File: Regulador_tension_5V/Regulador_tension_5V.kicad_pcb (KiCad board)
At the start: 2 copper layers, 53.6 x 29.2 mm, 10 parts, among them P1 CONN_01X02, P2 CONN_01X02, U1 LM7805

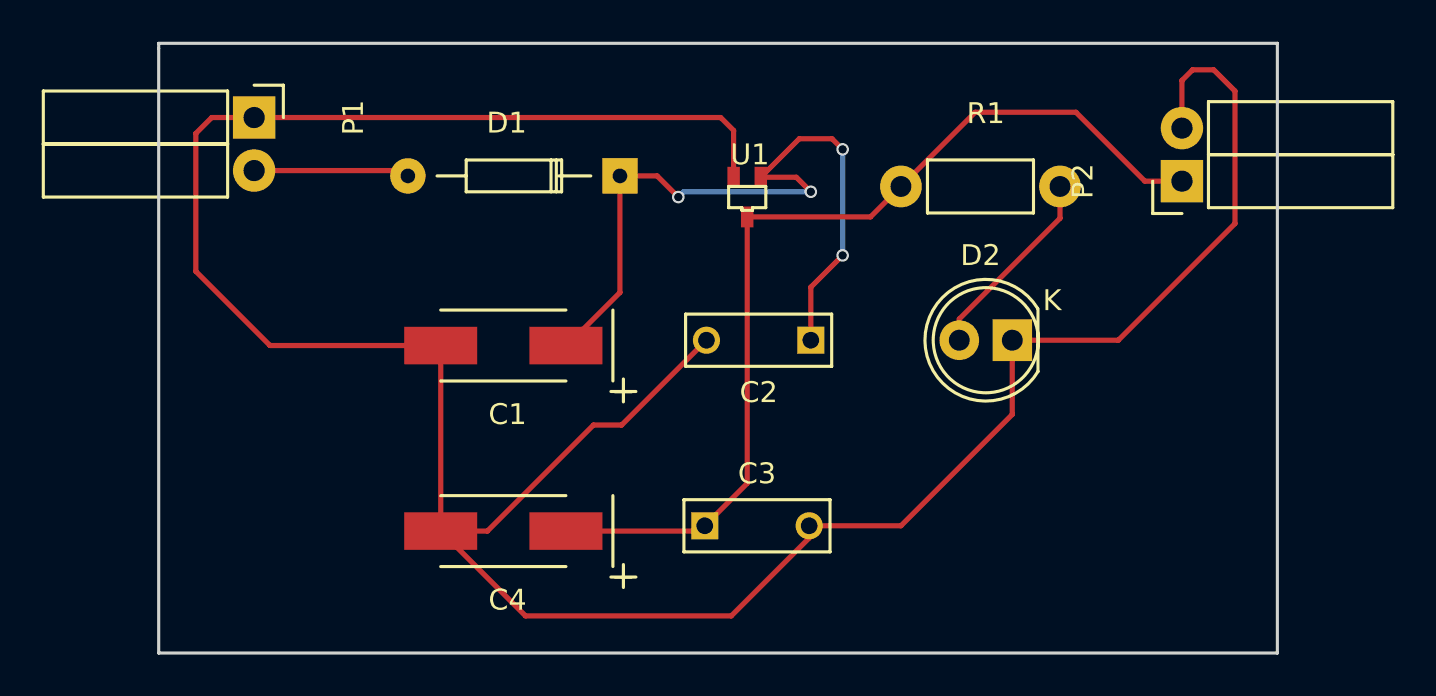
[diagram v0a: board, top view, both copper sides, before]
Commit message: Añadimos la versión 1.1 del regulador
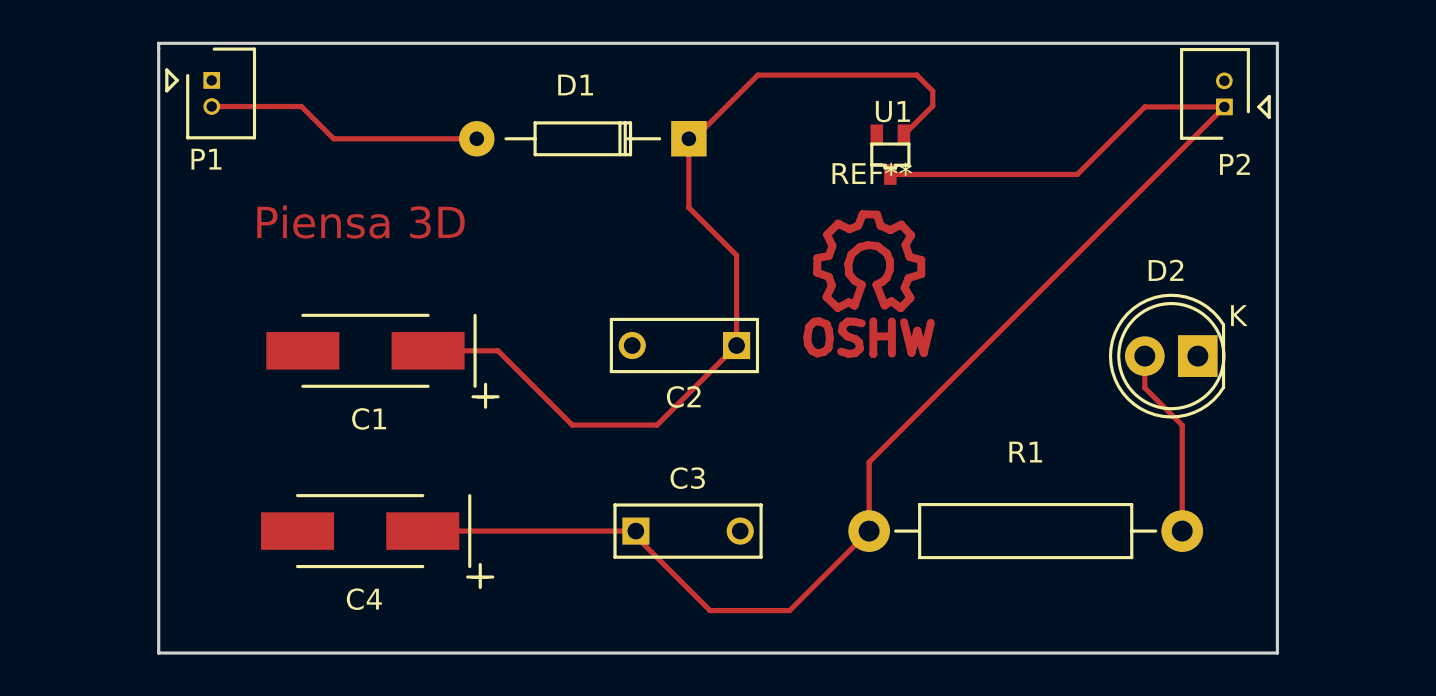
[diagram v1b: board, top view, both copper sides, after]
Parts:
- added REF**: Symbol_OSHW-Logo_CopperTop, Symbols:Symbol_OSHW-Logo_CopperTop, F.Cu at (134.4, 86.1)
- P1, P2: footprint Socket_Strips:Socket_Strip_Angled_1x02 -> Connectors_Molex:Connector_Molex_PicoBlade_53047-0210
- R1: footprint Resistors_ThroughHole:Resistor_Horizontal_RM7mm -> Resistors_ThroughHole:Resistor_Horizontal_RM15mm
- moved R1 16.6 mm to (134.4, 98.8)
- moved D2 8.92 mm to (150.1, 90.4)
- moved U1 7.15 mm to (135.4, 80.8)
- moved C4 6.86 mm to (110.0, 98.8)
- moved C1 6.61 mm to (110.2, 90.2)
- moved P2 4.10 mm to (151.4, 78.5)
- moved D1 3.75 mm to (125.7, 80.0)
- moved C2 3.57 mm to (128.0, 89.9)
- moved C3 3.31 mm to (123.2, 98.8)
- moved P1 2.70 mm to (102.9, 77.2)
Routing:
- net GND: track 135.6 -> 0.00 mm
- net Net-(C3-Pad1): track 46.7 -> 69.4 mm
- net Net-(C1-Pad1): track 36.3 -> 44.6 mm, vias 4 -> 0
- net Net-(D1-Pad2): track 7.47 -> 13.3 mm
- added copper zone on F.Cu, net GND
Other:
- board text added: "Piensa 3D"
